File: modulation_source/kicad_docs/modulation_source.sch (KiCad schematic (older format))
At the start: 73 parts, among them J1 power_in, Q1 BC560, Q2 BC560, Q3 BF245A, Q4 BC550, Q5 BC550, Q6 BC550, U1 LM13700, U2 TL072, U3 TL072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

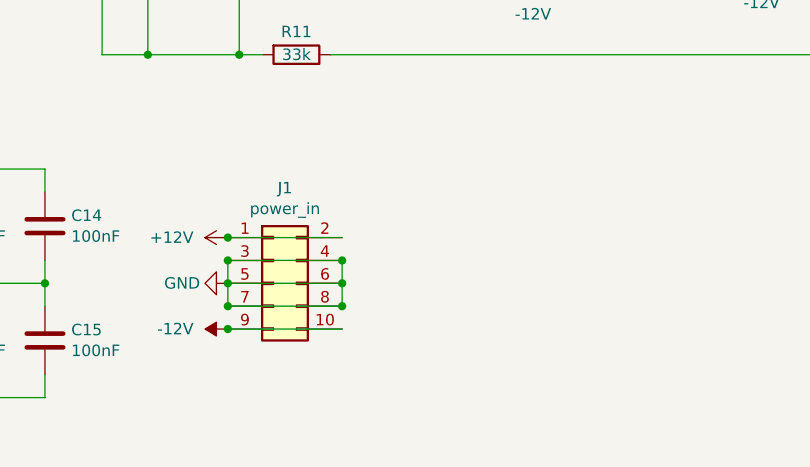
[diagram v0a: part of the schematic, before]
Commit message: add mod source title and schematic
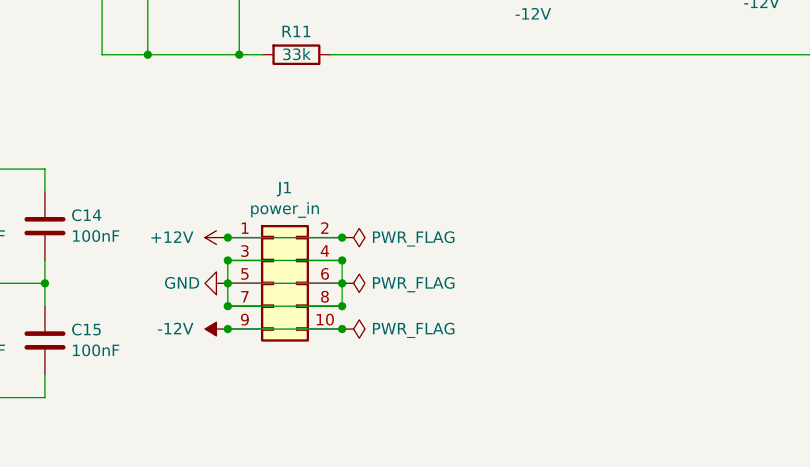
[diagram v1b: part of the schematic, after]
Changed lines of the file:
@@
 encoding utf-8
 Sheet 1 1
-Title ""
-Date ""
-Rev ""
+Title "Modulation Source"
+Date "2020-07-22"
+Rev "0"
 Comp ""
-Comment1 ""
-Comment2 ""
-Comment3 ""
+Comment1 "creativecommons.org/licenses/by/4.0/"
+Comment2 "License: CC by 4.0"
+Comment3 "Author: Jordan Aceto"
 Comment4 ""
 $EndDescr
@@
 	0    1    1    0
 $EndComp
+$Comp
+L power:PWR_FLAG #FLG0101
+U 1 1 5F19C27A
+P 6350 6800
+F 0 "#FLG0101" H 6350 6875 50  0001 C CNN
+F 1 "PWR_FLAG" V 6350 6928 50  0000 L CNN
+F 2 "" H 6350 6800 50  0001 C CNN
+F 3 "~" H 6350 6800 50  0001 C CNN
+	1    6350 6800
+	0    1    1    0
+$EndComp
+Connection ~ 6350 6800
+$Comp
+L power:PWR_FLAG #FLG0102
+U 1 1 5F19D617
+P 6350 7000
+F 0 "#FLG0102" H 6350 7075 50  0001 C CNN
+F 1 "PWR_FLAG" V 6350 7128 50  0000 L CNN
+F 2 "" H 6350 7000 50  0001 C CNN
+F 3 "~" H 6350 7000 50  0001 C CNN
+	1    6350 7000
+	0    1    1    0
+$EndComp
+$Comp
+L power:PWR_FLAG #FLG0103
+U 1 1 5F19D88A
+P 6350 7200
+F 0 "#FLG0103" H 6350 7275 50  0001 C CNN
+F 1 "PWR_FLAG" V 6350 7328 50  0000 L CNN
+F 2 "" H 6350 7200 50  0001 C CNN
+F 3 "~" H 6350 7200 50  0001 C CNN
+	1    6350 7200
+	0    1    1    0
+$EndComp
+Connection ~ 6350 7200
 $EndSCHEMATC
